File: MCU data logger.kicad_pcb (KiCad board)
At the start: 2 copper layers, 53.1 x 35.5 mm, 29 parts, among them J1 Conn_01x04_Pin, J2 Conn_01x04_Pin, J3 Conn_01x09_Pin, J4 Conn_02x03_Odd_Even, U1 ATMEGA328P-AN, U2 DS1337S_, U3 24LC1025, U4 24LC1025, Y1 32.768Khz, Y2 16MHz

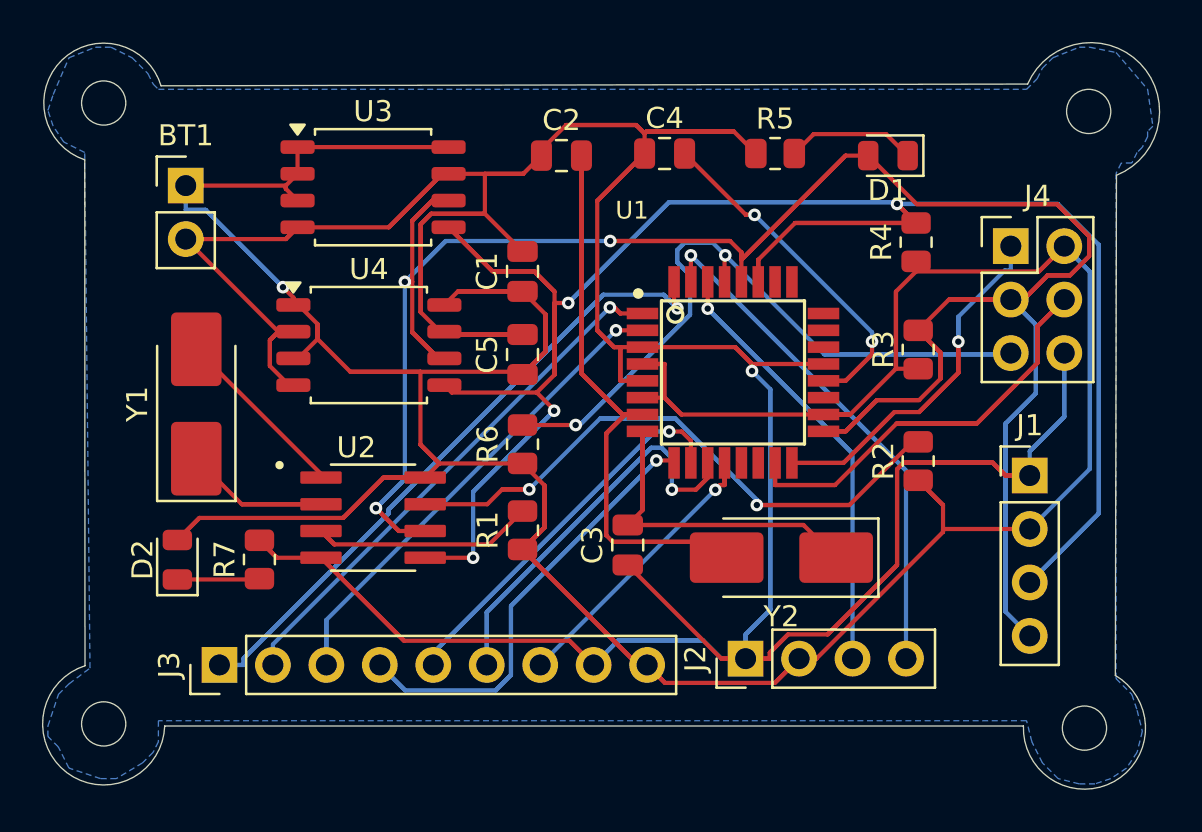
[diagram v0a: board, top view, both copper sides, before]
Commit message: Converted PCB to 4-layer stackup
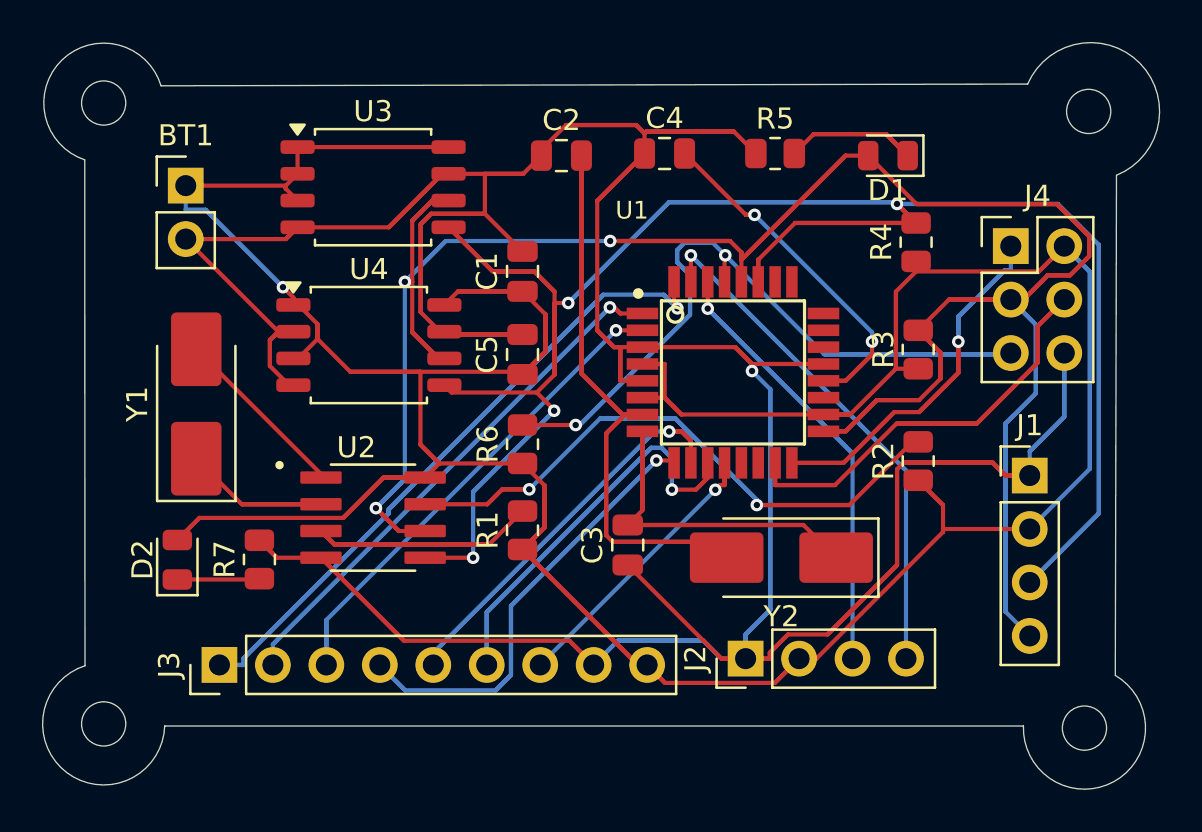
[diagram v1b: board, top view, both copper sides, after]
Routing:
- net /D3: track 25.9 -> 48.8 mm
- net Net-(U2-~{INTA}): track 11.4 -> 18.7 mm
- net Net-(D1-K): track 6.19 -> 12.5 mm
- net /MISO: track 28.1 -> 31.5 mm
- net /D6: track 33.9 -> 35.6 mm
- net GND: track 246.7 -> 247.8 mm
- net Net-(U2-SQW/~INT): track 43.4 -> 44.4 mm
- added copper zone on In1.Cu, net GND
- added copper zone on In2.Cu, net VCC
- removed copper zone on B.Cu, net GND
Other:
- copper layers 2 -> 4
